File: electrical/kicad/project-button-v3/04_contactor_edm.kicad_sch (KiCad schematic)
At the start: 4 parts, among them K1 Schneider TeSys D LC1D25BD, 2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, K2 Schneider TeSys D LC1D25BD, 2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

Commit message: Add native DYNAMIXEL star injection release candidate
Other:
- title: PB HR-V0 Electrical V3 - 04 -> PB HR-V0 V3-P1.2 - 04
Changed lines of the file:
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@@
   (version 20250114) (generator "eeschema") (generator_version "10.0")
  (paper "A3")
-  (title_block (title "PB HR-V0 Electrical V3 - 04") (date "2026-08-06") (rev "V3-P1.1")
+  (title_block (title "PB HR-V0 V3-P1.2 - 04") (date "2026-08-07") (rev "V3-P1.2")
     (company "Project Button") (comment 1 "PRELIMINARY - NOT APPROVED FOR FABRICATION OR ENERGIZATION") (comment 2 "CONNECTED DESIGN CANDIDATE - QUALIFIED REVIEW REQUIRED"))
   (text "PRELIMINARY - NOT APPROVED FOR FABRICATION OR ENERGIZATION" (exclude_from_sim no) (at 17.78 10.16 0)

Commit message: Document HR-V0 contactor application evidence
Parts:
- K1: Evidence Schneider product sheet rechecked 2026-08-06; loaded DC int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 -> Schneider MKTED210011EN Catalog 2026 pp. A5/120-A5/123, LC1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; Status PROPOSED - DC APPLICATION CONFIRMATION REQUIRED -> PROPOSED - CATALOG DC ENVELOPE FOUND; CRITICAL-CURRENT AND 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
- K2: Evidence (none) -> Schneider MKTED210011EN Catalog 2026 pp. A5/120-A5/123, LC1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; Status PROPOSED - DC APPLICATION CONFIRMATION REQUIRED -> PROPOSED - CATALOG DC ENVELOPE FOUND; CRITICAL-CURRENT AND 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
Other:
- title: PB HR-V0 V3-P1.2 - 04 -> PB HR-V0 V3-P1.3 - 04
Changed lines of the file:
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@@
   (version 20250114) (generator "eeschema") (generator_version "10.0")
  (paper "A3")
-  (title_block (title "PB HR-V0 V3-P1.2 - 04") (date "2026-08-07") (rev "V3-P1.2")
+  (title_block (title "PB HR-V0 V3-P1.3 - 04") (date "2026-08-07") (rev "V3-P1.3")
     (company "Project Button") (comment 1 "PRELIMINARY - NOT APPROVED FOR FABRICATION OR ENERGIZATION") (comment 2 "CONNECTED DESIGN CANDIDATE - QUALIFIED REVIEW REQUIRED"))
   (text "PRELIMINARY - NOT APPROVED FOR FABRICATION OR ENERGIZATION" (exclude_from_sim no) (at 17.78 10.16 0)
@@
       (property "Value" "Schneider TeSys D LC1D25BD, 24 VDC coil" (at 95.25 85.09 0) (effects (font (size 1.50 1.50)) (hide yes)))
       (property "Footprint" "" (at 95.25 85.09 0) (effects (font (size 1.50 1.50)) (hide yes)))
-      (property "Datasheet" "https://iportal.se.com/Contents/docs/SQD-LC1D25BD.PDF" (at 95.25 85.09 0) (effects (font (size 1.50 1.50)) (hide yes)))
-      (property "Description" "First redundant series contactor. BD coil has built-in bidirectional peak-limiting diode; do not add assumed external suppression." (at 95.25 85.09 0) (effects (font (size 1.50 1.50)) (hide yes)))
-      (property "Status" "PROPOSED - DC APPLICATION CONFIRMATION REQUIRED" (at 95.25 100.79 0) (effects (font (size 1.50 1.50)) (justify bottom)))
-      (property "Evidence" "Schneider product sheet rechecked 2026-08-06; loaded DC interruption/coordination not established." (at 95.25 85.09 0) (effects (font (size 1.50 1.50)) (hide yes)))
+      (property "Datasheet" "https://download.schneider-electric.com/files?filename=Catalog&p_Doc_Ref=MKTED210011EN" (at 95.25 85.09 0) (effects (font (size 1.50 1.50)) (hide yes)))
+      (property "Description" "First redundant series contactor. Three power poles are represented in series. The 2026 catalog's LC1D25 24 V row is 32 A for one, two or three poles, but its lower-current critical-current warning applies to the 11.1 A HR-V0 screen. BD coil has built-in bidirectional peak-limiting diode; do not add assumed external suppression." (at 95.25 85.09 0) (effects (font (size 1.50 1.50)) (hide yes)))
+      (property "Status" "PROPOSED - CATALOG DC ENVELOPE FOUND; CRITICAL-CURRENT AND APPLICATION CONFIRMATION REQUIRED; TEST REQUIRED" (at 95.25 100.79 0) (effects (font (size 1.50 1.50)) (justify bottom)))
+      (property "Evidence" "Schneider MKTED210011EN Catalog 2026 pp. A5/120-A5/123, LC1D25BD product sheet dated 2017-09-13, and FA126437 modified 2026-05-12; rechecked 2026-08-07. Loaded DC interruption, critical-current disposition and coordination remain open." (at 95.25 85.09 0) (effects (font (size 1.50 1.50)) (hide yes)))
       (property "Display" "Schneider TeSys D LC1D25BD, 24 VDC coil" (at 54.61 71.59 0) (effects (font (size 1.50 1.50)) (justify left bottom)))
       (pin "A1")
@@
       (property "Value" "Schneider TeSys D LC1D25BD, 24 VDC coil" (at 299.72 85.09 0) (effects (font (size 1.50 1.50)) (hide yes)))
       (property "Footprint" "" (at 299.72 85.09 0) (effects (font (size 1.50 1.50)) (hide yes)))
-      (property "Datasheet" "https://iportal.se.com/Contents/docs/SQD-LC1D25BD.PDF" (at 299.72 85.09 0) (effects (font (size 1.50 1.50)) (hide yes)))
-      (property "Description" "Second redundant series contactor." (at 299.72 85.09 0) (effects (font (size 1.50 1.50)) (hide yes)))
-      (property "Status" "PROPOSED - DC APPLICATION CONFIRMATION REQUIRED" (at 299.72 100.79 0) (effects (font (size 1.50 1.50)) (justify bottom)))
-      (property "Evidence" "" (at 299.72 85.09 0) (effects (font (size 1.50 1.50)) (hide yes)))
+      (property "Datasheet" "https://download.schneider-electric.com/files?filename=Catalog&p_Doc_Ref=MKTED210011EN" (at 299.72 85.09 0) (effects (font (size 1.50 1.50)) (hide yes)))
+      (property "Description" "Second redundant series contactor. Same three-pole series application boundary, critical-current warning and physical evidence gate as K1." (at 299.72 85.09 0) (effects (font (size 1.50 1.50)) (hide yes)))
+      (property "Status" "PROPOSED - CATALOG DC ENVELOPE FOUND; CRITICAL-CURRENT AND APPLICATION CONFIRMATION REQUIRED; TEST REQUIRED" (at 299.72 100.79 0) (effects (font (size 1.50 1.50)) (justify bottom)))
+      (property "Evidence" "Schneider MKTED210011EN Catalog 2026 pp. A5/120-A5/123, LC1D25BD product sheet dated 2017-09-13, and FA126437 modified 2026-05-12; rechecked 2026-08-07." (at 299.72 85.09 0) (effects (font (size 1.50 1.50)) (hide yes)))
       (property "Display" "Schneider TeSys D LC1D25BD, 24 VDC coil" (at 259.08 71.59 0) (effects (font (size 1.50 1.50)) (justify left bottom)))
       (pin "A1")

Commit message: Add received-lot control for reset and arm terminals
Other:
- title: PB HR-V0 V3-P1.3 - 04 -> PB HR-V0 V3-P1.4 - 04
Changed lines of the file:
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@@
   (version 20250114) (generator "eeschema") (generator_version "10.0")
  (paper "A3")
-  (title_block (title "PB HR-V0 V3-P1.3 - 04") (date "2026-08-07") (rev "V3-P1.3")
+  (title_block (title "PB HR-V0 V3-P1.4 - 04") (date "2026-08-07") (rev "V3-P1.4")
     (company "Project Button") (comment 1 "PRELIMINARY - NOT APPROVED FOR FABRICATION OR ENERGIZATION") (comment 2 "CONNECTED DESIGN CANDIDATE - QUALIFIED REVIEW REQUIRED"))
   (text "PRELIMINARY - NOT APPROVED FOR FABRICATION OR ENERGIZATION" (exclude_from_sim no) (at 17.78 10.16 0)

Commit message: Reconcile H1 pilot light in electrical V3
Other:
- title: PB HR-V0 V3-P1.4 - 04 -> PB HR-V0 V3-P1.5 - 04
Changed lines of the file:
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@@
   (version 20250114) (generator "eeschema") (generator_version "10.0")
  (paper "A3")
-  (title_block (title "PB HR-V0 V3-P1.4 - 04") (date "2026-08-07") (rev "V3-P1.4")
+  (title_block (title "PB HR-V0 V3-P1.5 - 04") (date "2026-08-07") (rev "V3-P1.5")
     (company "Project Button") (comment 1 "PRELIMINARY - NOT APPROVED FOR FABRICATION OR ENERGIZATION") (comment 2 "CONNECTED DESIGN CANDIDATE - QUALIFIED REVIEW REQUIRED"))
   (text "PRELIMINARY - NOT APPROVED FOR FABRICATION OR ENERGIZATION" (exclude_from_sim no) (at 17.78 10.16 0)

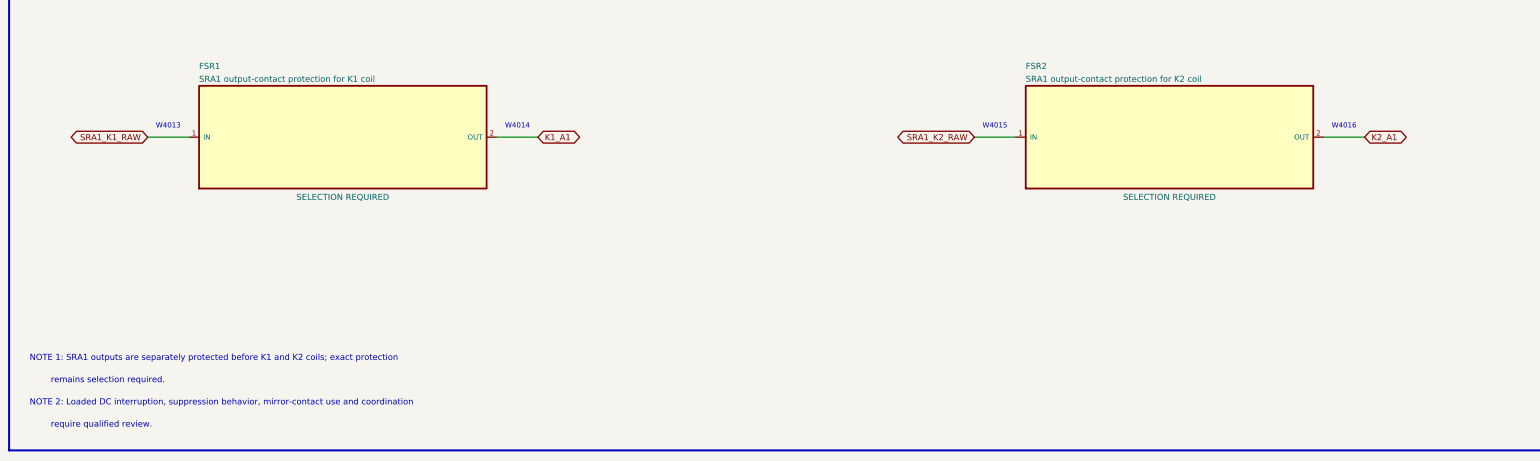
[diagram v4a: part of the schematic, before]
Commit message: Correct control-panel protection fit
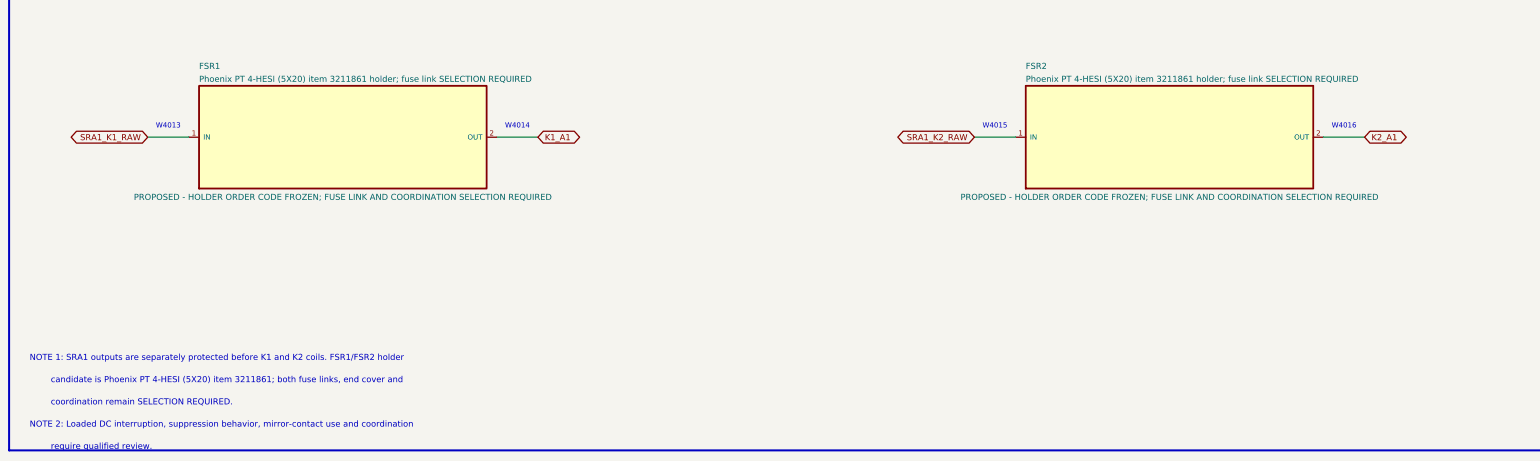
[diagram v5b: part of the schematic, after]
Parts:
- FSR1: value SRA1 output-contact protection for K1 coil -> Phoenix PT 4-HESI (5X20) item 3211861 holder; fuse link SELECTION REQUIRED; Display SRA1 output-contact protection for K1 coil -> Phoenix PT 4-HESI (5X20) item 3211861 holder; fuse link SEL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; Evidence (none) -> Phoenix Contact official US product page and generated prod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; Status SELECTION REQUIRED -> PROPOSED - HOLDER ORDER CODE FROZEN; FUSE LINK AND COORDINA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
- FSR2: value SRA1 output-contact protection for K2 coil -> Phoenix PT 4-HESI (5X20) item 3211861 holder; fuse link SELECTION REQUIRED; Display SRA1 output-contact protection for K2 coil -> Phoenix PT 4-HESI (5X20) item 3211861 holder; fuse link SEL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; Evidence (none) -> Phoenix Contact official US product page and generated prod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; Status SELECTION REQUIRED -> PROPOSED - HOLDER ORDER CODE FROZEN; FUSE LINK AND COORDINA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
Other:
- note added: "NOTE 1: SRA1 outputs are separately protected before K1 and K2 coils. FSR1/FSR2 holder"
- note added: "candidate is Phoenix PT 4-HESI (5X20) item 3211861; both fuse links, end cover and"
- note added: "coordination remain SELECTION REQUIRED."
- note removed: "NOTE 1: SRA1 outputs are separately protected before K1 and K2 coils; exact protection"
- note removed: "remains selection required."
- title: PB HR-V0 V3-P1.5 - 04 -> PB HR-V0 V3-P1.6 - 04
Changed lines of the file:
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@@
   (version 20250114) (generator "eeschema") (generator_version "10.0")
  (paper "A3")
-  (title_block (title "PB HR-V0 V3-P1.5 - 04") (date "2026-08-07") (rev "V3-P1.5")
+  (title_block (title "PB HR-V0 V3-P1.6 - 04") (date "2026-08-07") (rev "V3-P1.6")
     (company "Project Button") (comment 1 "PRELIMINARY - NOT APPROVED FOR FABRICATION OR ENERGIZATION") (comment 2 "CONNECTED DESIGN CANDIDATE - QUALIFIED REVIEW REQUIRED"))
   (text "PRELIMINARY - NOT APPROVED FOR FABRICATION OR ENERGIZATION" (exclude_from_sim no) (at 17.78 10.16 0)
@@
 (text "W4016" (exclude_from_sim no)
               (at 342.90 202.47 0) (effects (font (size 1.27 1.27)) (justify bottom))
-) (text "NOTE 1: SRA1 outputs are separately protected before K1 and K2 coils; exact protection" (exclude_from_sim no) (at 17.78 260.00 0)
-      (effects (font (size 1.50 1.50)) (justify left bottom))) (text "        remains selection required." (exclude_from_sim no) (at 17.78 265.50 0)
-      (effects (font (size 1.50 1.50)) (justify left bottom))) (text "NOTE 2: Loaded DC interruption, suppression behavior, mirror-contact use and coordination" (exclude_from_sim no) (at 17.78 271.00 0)
-      (effects (font (size 1.50 1.50)) (justify left bottom))) (text "        require qualified review." (exclude_from_sim no) (at 17.78 276.50 0)
+) (text "NOTE 1: SRA1 outputs are separately protected before K1 and K2 coils. FSR1/FSR2 holder" (exclude_from_sim no) (at 17.78 260.00 0)
+      (effects (font (size 1.50 1.50)) (justify left bottom))) (text "        candidate is Phoenix PT 4-HESI (5X20) item 3211861; both fuse links, end cover and" (exclude_from_sim no) (at 17.78 265.50 0)
+      (effects (font (size 1.50 1.50)) (justify left bottom))) (text "        coordination remain SELECTION REQUIRED." (exclude_from_sim no) (at 17.78 271.00 0)
+      (effects (font (size 1.50 1.50)) (justify left bottom))) (text "NOTE 2: Loaded DC interruption, suppression behavior, mirror-contact use and coordination" (exclude_from_sim no) (at 17.78 276.50 0)
+      (effects (font (size 1.50 1.50)) (justify left bottom))) (text "        require qualified review." (exclude_from_sim no) (at 17.78 282.00 0)
       (effects (font (size 1.50 1.50)) (justify left bottom)))
   (symbol
@@
       (exclude_from_sim no) (in_bom yes) (on_board yes) (dnp no)
       (property "Reference" "FSR1" (at 59.69 187.77 0) (effects (font (size 1.50 1.50)) (justify left bottom)))
-      (property "Value" "SRA1 output-contact protection for K1 coil" (at 95.25 204.47 0) (effects (font (size 1.50 1.50)) (hide yes)))
+      (property "Value" "Phoenix PT 4-HESI (5X20) item 3211861 holder; fuse link SELECTION REQUIRED" (at 95.25 204.47 0) (effects (font (size 1.50 1.50)) (hide yes)))
       (property "Footprint" "" (at 95.25 204.47 0) (effects (font (size 1.50 1.50)) (hide yes)))
-      (property "Datasheet" "" (at 95.25 204.47 0) (effects (font (size 1.50 1.50)) (hide yes)))
-      (property "Description" "R36 input register exists, but exact device/holder, fault current, coil pickup/transient, conductor and PNOZ contact-protection coordination remain open; published maxima are not selections." (at 95.25 204.47 0) (effects (font (size 1.50 1.50)) (hide yes)))
-      (property "Status" "SELECTION REQUIRED" (at 95.25 220.17 0) (effects (font (size 1.50 1.50)) (justify bottom)))
-      (property "Evidence" "" (at 95.25 204.47 0) (effects (font (size 1.50 1.50)) (hide yes)))
-      (property "Display" "SRA1 output-contact protection for K1 coil" (at 59.69 190.97 0) (effects (font (size 1.50 1.50)) (justify left bottom)))
+      (property "Datasheet" "https://www.phoenixcontact.com/en-us/products/fuse-terminal-block-pt-4-hesi-5x20-3211861" (at 95.25 204.47 0) (effects (font (size 1.50 1.50)) (hide yes)))
+      (property "Description" "Exact non-LED 5x20 holder candidate only. Fuse link, compatible end cover, fault current, coil pickup/transient, conductor and PNOZ contact-protection coordination remain open; manufacturer maxima are not project selections." (at 95.25 204.47 0) (effects (font (size 1.50 1.50)) (hide yes)))
+      (property "Status" "PROPOSED - HOLDER ORDER CODE FROZEN; FUSE LINK AND COORDINATION SELECTION REQUIRED" (at 95.25 220.17 0) (effects (font (size 1.50 1.50)) (justify bottom)))
+      (property "Evidence" "Phoenix Contact official US product page and generated product PDF dated 2026-07-06; rechecked 2026-08-07." (at 95.25 204.47 0) (effects (font (size 1.50 1.50)) (hide yes)))
+      (property "Display" "Phoenix PT 4-HESI (5X20) item 3211861 holder; fuse link SELECTION REQUIRED" (at 59.69 190.97 0) (effects (font (size 1.50 1.50)) (justify left bottom)))
       (pin "1")
       (pin "2")
@@
       (exclude_from_sim no) (in_bom yes) (on_board yes) (dnp no)
       (property "Reference" "FSR2" (at 264.16 187.77 0) (effects (font (size 1.50 1.50)) (justify left bottom)))
-      (property "Value" "SRA1 output-contact protection for K2 coil" (at 299.72 204.47 0) (effects (font (size 1.50 1.50)) (hide yes)))
+      (property "Value" "Phoenix PT 4-HESI (5X20) item 3211861 holder; fuse link SELECTION REQUIRED" (at 299.72 204.47 0) (effects (font (size 1.50 1.50)) (hide yes)))
       (property "Footprint" "" (at 299.72 204.47 0) (effects (font (size 1.50 1.50)) (hide yes)))
-      (property "Datasheet" "" (at 299.72 204.47 0) (effects (font (size 1.50 1.50)) (hide yes)))
-      (property "Description" "Same R36 coordination and physical-evidence gate as FSR1." (at 299.72 204.47 0) (effects (font (size 1.50 1.50)) (hide yes)))
-      (property "Status" "SELECTION REQUIRED" (at 299.72 220.17 0) (effects (font (size 1.50 1.50)) (justify bottom)))
-      (property "Evidence" "" (at 299.72 204.47 0) (effects (font (size 1.50 1.50)) (hide yes)))
-      (property "Display" "SRA1 output-contact protection for K2 coil" (at 264.16 190.97 0) (effects (font (size 1.50 1.50)) (justify left bottom)))
+      (property "Datasheet" "https://www.phoenixcontact.com/en-us/products/fuse-terminal-block-pt-4-hesi-5x20-3211861" (at 299.72 204.47 0) (effects (font (size 1.50 1.50)) (hide yes)))
+      (property "Description" "Same exact holder candidate and open fuse-link, end-cover, coordination and physical-evidence gate as FSR1." (at 299.72 204.47 0) (effects (font (size 1.50 1.50)) (hide yes)))
+      (property "Status" "PROPOSED - HOLDER ORDER CODE FROZEN; FUSE LINK AND COORDINATION SELECTION REQUIRED" (at 299.72 220.17 0) (effects (font (size 1.50 1.50)) (justify bottom)))
+      (property "Evidence" "Phoenix Contact official US product page and generated product PDF dated 2026-07-06; rechecked 2026-08-07." (at 299.72 204.47 0) (effects (font (size 1.50 1.50)) (hide yes)))
+      (property "Display" "Phoenix PT 4-HESI (5X20) item 3211861 holder; fuse link SELECTION REQUIRED" (at 264.16 190.97 0) (effects (font (size 1.50 1.50)) (justify left bottom)))
       (pin "1")
       (pin "2")
